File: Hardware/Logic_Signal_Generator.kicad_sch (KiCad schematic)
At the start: 10 parts, among them J1 JTAG, J3 USB_B, U1 PIC18F25K50-xSO

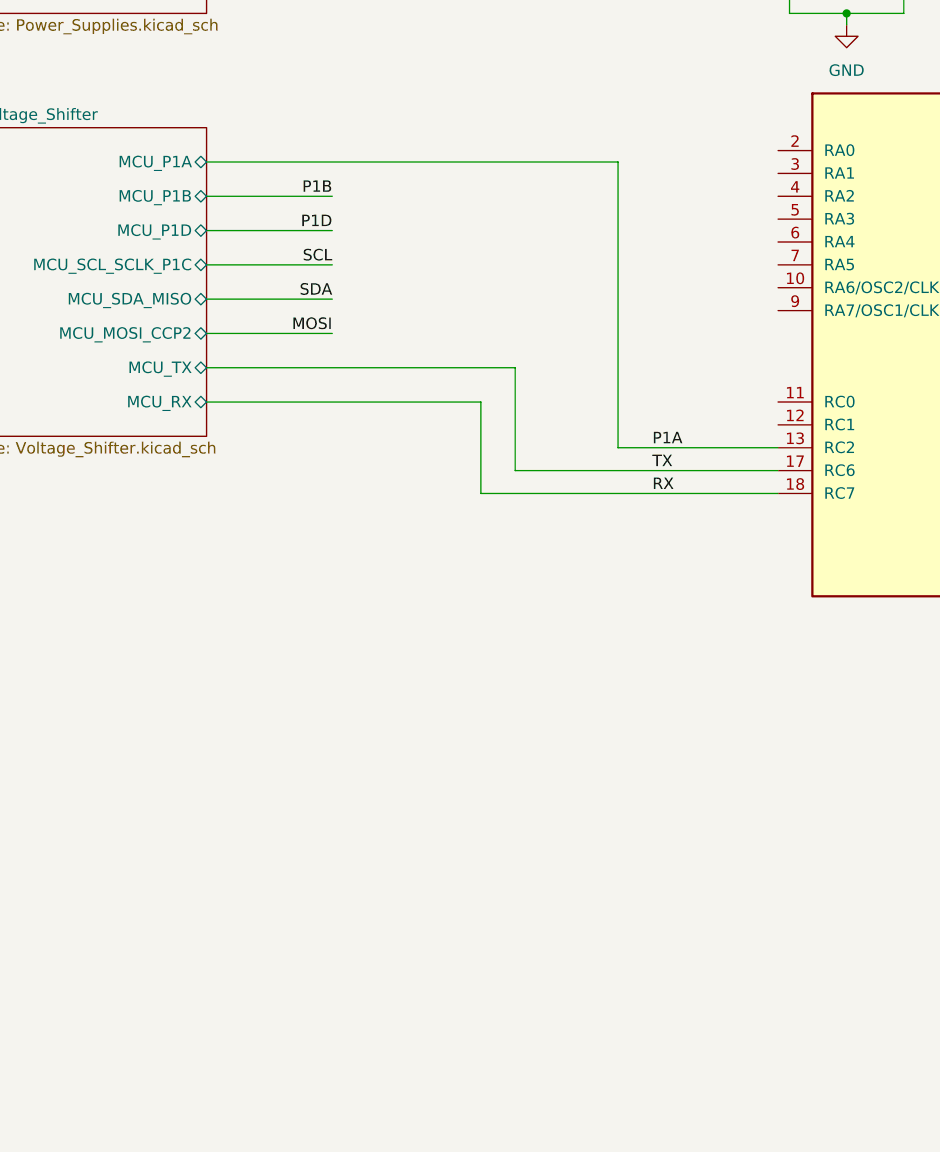
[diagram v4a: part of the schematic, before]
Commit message: [Hardware] Added the power and USB activity LEDs to the schematic.
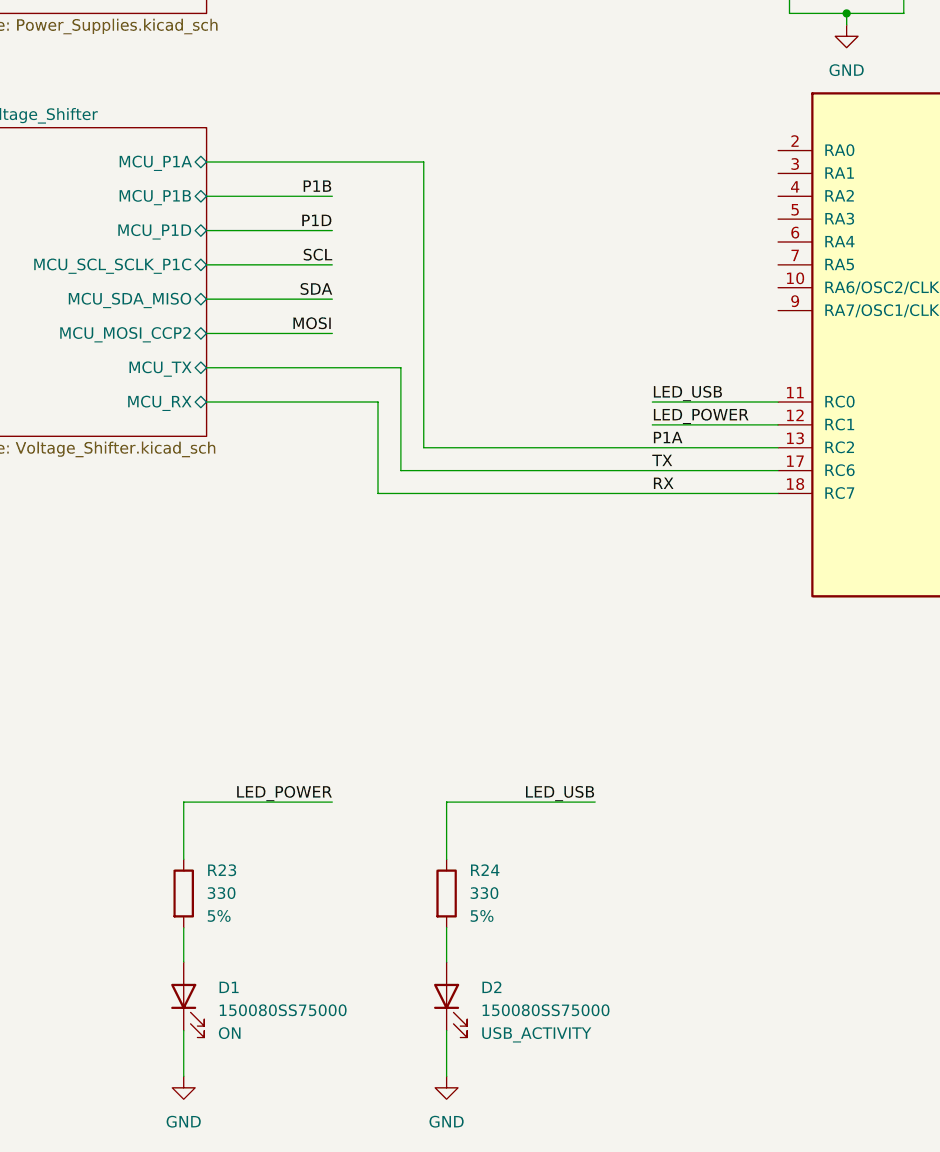
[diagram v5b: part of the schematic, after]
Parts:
- added D1, D2: 150080SS75000, LED_SMD:LED_0805_2012Metric_Pad1.15x1.40mm_HandSolder, symbol Device:LED
- added R23, R24: 330, Resistor_SMD:R_0603_1608Metric_Pad0.98x0.95mm_HandSolder, symbol Device:R
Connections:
- net GND: now also D1.1 (K), D2.1 (K)
- net LED_USB: now reaches U1.11 (RC0)
- net LED_USB: now also R24.1
- net LED_POWER: now reaches U1.12 (RC1)
- net LED_POWER: now also R23.1
- new net: D2.2 (A), R24.2
- new net: D1.2 (A), R23.2

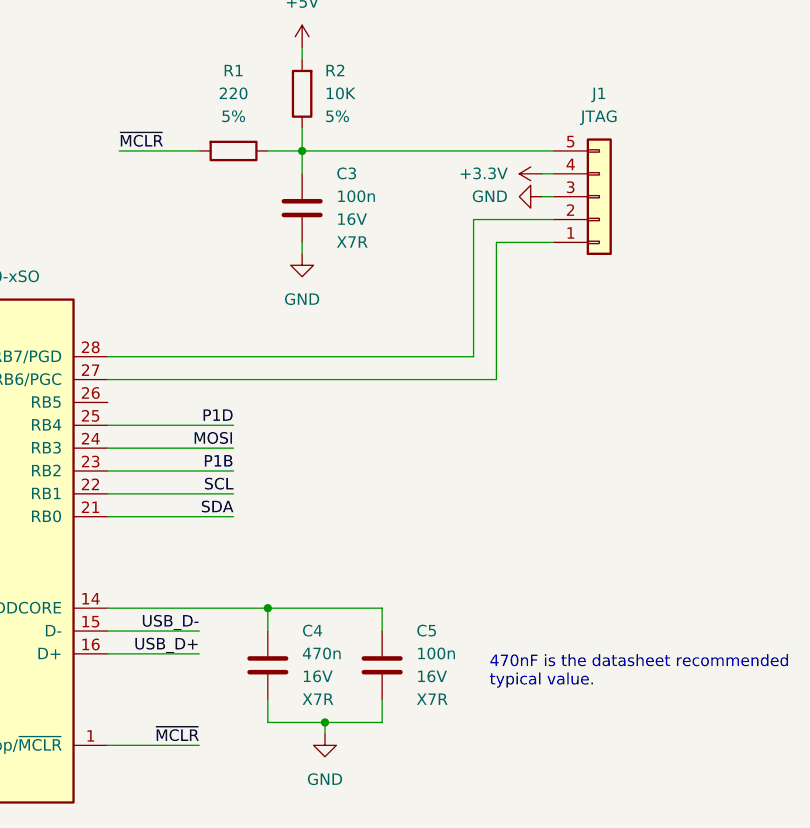
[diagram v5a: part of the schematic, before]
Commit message: [Hardware] Made an initial placement of the components on the PCB.
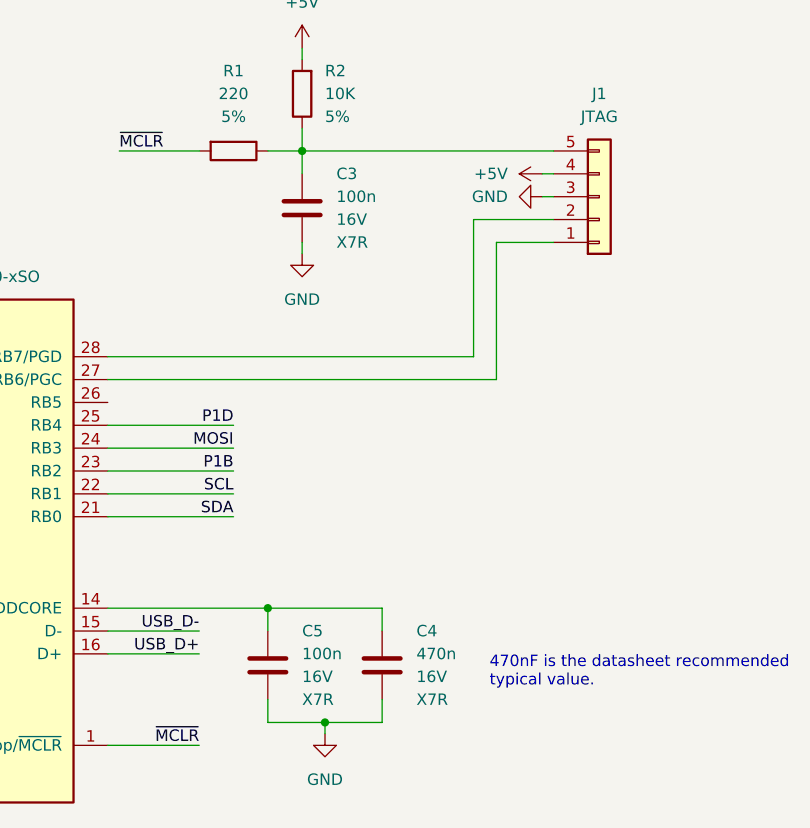
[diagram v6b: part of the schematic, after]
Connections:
- net +3.3V is gone; now on net +5V: J1.4 (Pin_4)
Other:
- moved on the sheet: C4, C5
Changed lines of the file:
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@@
+	)
+	(symbol
+		(lib_id "power:+5V")
+		(at 213.36 45.72 90)
+		(unit 1)
+		(exclude_from_sim no)
+		(in_bom yes)
+		(on_board yes)
+		(dnp no)
+		(fields_autoplaced yes)
+		(property "Reference" "#PWR039"
+			(at 217.17 45.72 0)
+			(effects
+				(font
+					(size 1.27 1.27)
+				)
+				(hide yes)
+			)
+		)
+		(property "Value" "+5V"
+			(at 209.55 45.7199 90)
+			(effects
+				(font
+					(size 1.27 1.27)
+				)
+				(justify left)
+			)
+		)
+		(property "Footprint" ""
+			(at 213.36 45.72 0)
+			(effects
+				(font
+					(size 1.27 1.27)
+				)
+				(hide yes)
+			)
+		)
+		(property "Datasheet" ""
+			(at 213.36 45.72 0)
+			(effects
+				(font
+					(size 1.27 1.27)
+				)
+				(hide yes)
+			)
+		)
+		(property "Description" "Power symbol creates a global label with name \"+5V\""
+			(at 213.36 45.72 0)
+			(effects
+				(font
+					(size 1.27 1.27)
+				)
+				(hide yes)
+			)
+		)
+		(pin "1"
+		)
+		(instances
+			(project "Logic_Signal_Generator"
+				(path "/24489a00-9deb-415a-805c-b5419253b078"
+					(reference "#PWR039")
+					(unit 1)
+				)
+			)
+		)
 	)
 	(symbol
@@
 	(symbol
 		(lib_id "Device:C")
-		(at 195.58 100.33 0)
+		(at 182.88 100.33 0)
 		(unit 1)
 		(exclude_from_sim no)
@@
 		(fields_autoplaced yes)
 		(property "Reference" "C5"
-			(at 199.39 96.5199 0)
+			(at 186.69 96.5199 0)
 			(effects
 				(font
@@
 		)
 		(property "Value" "100n"
-			(at 199.39 99.0599 0)
+			(at 186.69 99.0599 0)
 			(effects
 				(font
@@
 		)
 		(property "Footprint" "Capacitor_SMD:C_0603_1608Metric_Pad1.08x0.95mm_HandSolder"
-			(at 196.5452 104.14 0)
+			(at 183.8452 104.14 0)
 			(effects
 				(font
@@
 		)
 		(property "Datasheet" "~"
-			(at 195.58 100.33 0)
+			(at 182.88 100.33 0)
 			(effects
 				(font
@@
 		)
 		(property "Description" ""
-			(at 195.58 100.33 0)
+			(at 182.88 100.33 0)
 			(effects
 				(font
@@
 		)
 		(property "Value2" "16V"
-			(at 199.39 101.5999 0)
+			(at 186.69 101.5999 0)
 			(effects
 				(font
@@
 		)
 		(property "Value3" "X7R"
-			(at 199.39 104.1399 0)
+			(at 186.69 104.1399 0)
 			(effects
 				(font
@@
 	)
 	(symbol
-		(lib_id "power:+3.3V")
-		(at 213.36 45.72 90)
-		(unit 1)
-		(exclude_from_sim no)
-		(in_bom yes)
-		(on_board yes)
-		(dnp no)
-		(fields_autoplaced yes)
-		(property "Reference" "#PWR039"
-			(at 217.17 45.72 0)
-			(effects
-				(font
-					(size 1.27 1.27)
-				)
-				(hide yes)
-			)
-		)
-		(property "Value" "+3.3V"
-			(at 209.55 45.72 90)
-			(effects
-				(font
-					(size 1.27 1.27)
-				)
-				(justify left)
-			)
-		)
-		(property "Footprint" ""
-			(at 213.36 45.72 0)
-			(effects
-				(font
-					(size 1.27 1.27)
-				)
-				(hide yes)
-			)
-		)
-		(property "Datasheet" ""
-			(at 213.36 45.72 0)
-			(effects
-				(font
-					(size 1.27 1.27)
-				)
-				(hide yes)
-			)
-		)
-		(property "Description" "Power symbol creates a global label with name \"+3.3V\""
-			(at 213.36 45.72 0)
-			(effects
-				(font
-					(size 1.27 1.27)
-				)
-				(hide yes)
-			)
-		)
-		(pin "1"
-		)
-		(instances
-			(project "Logic_Signal_Generator"
-				(path "/24489a00-9deb-415a-805c-b5419253b078"
-					(reference "#PWR039")
-					(unit 1)
-				)
-			)
-		)
-	)
-	(symbol
 		(lib_id "Device:C")
 		(at 186.69 49.53 0)
@@
 	(symbol
 		(lib_id "Device:C")
-		(at 182.88 100.33 0)
+		(at 195.58 100.33 0)
 		(unit 1)
 		(exclude_from_sim no)
@@
 		(fields_autoplaced yes)
 		(property "Reference" "C4"
-			(at 186.69 96.5199 0)
+			(at 199.39 96.5199 0)
 			(effects
 				(font
@@
 		)
 		(property "Value" "470n"
-			(at 186.69 99.0599 0)
+			(at 199.39 99.0599 0)
 			(effects
 				(font
@@
 		)
 		(property "Footprint" "Capacitor_SMD:C_0603_1608Metric_Pad1.08x0.95mm_HandSolder"
-			(at 183.8452 104.14 0)
+			(at 196.5452 104.14 0)
 			(effects
 				(font
@@
 		)
 		(property "Datasheet" "~"
-			(at 182.88 100.33 0)
+			(at 195.58 100.33 0)
 			(effects
 				(font
@@
 		)
 		(property "Description" "Unpolarized capacitor"
-			(at 182.88 100.33 0)
+			(at 195.58 100.33 0)
 			(effects
 				(font
@@
 		)
 		(property "Value2" "16V"
-			(at 186.69 101.5999 0)
+			(at 199.39 101.5999 0)
 			(effects
 				(font
@@
 		)
 		(property "Value3" "X7R"
-			(at 186.69 104.1399 0)
-			(effects
-				(font
+			(at 199.39 104.1399 0)
+			(effects
+				(font

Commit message: [Hardware] Added the mounting holes and the PCB edges.
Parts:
- added H1, H2, H3, H4: Hole, MountingHole:MountingHole_4.5mm_Pad_Via, symbol Mechanical:MountingHole_Pad
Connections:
- net GND: now also H1.1, H2.1, H3.1, H4.1

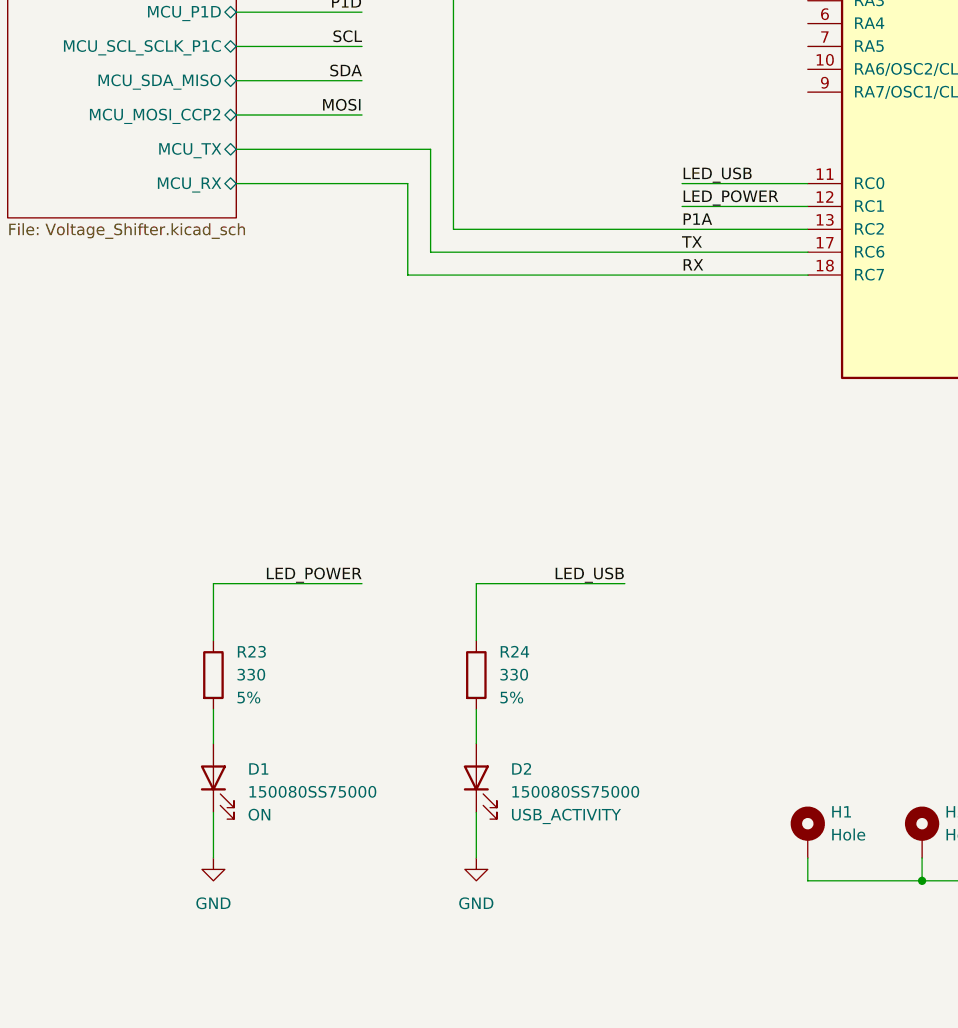
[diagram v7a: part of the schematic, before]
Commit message: [Hardware] Routed the LEDs and changed their current limiting resistors package.
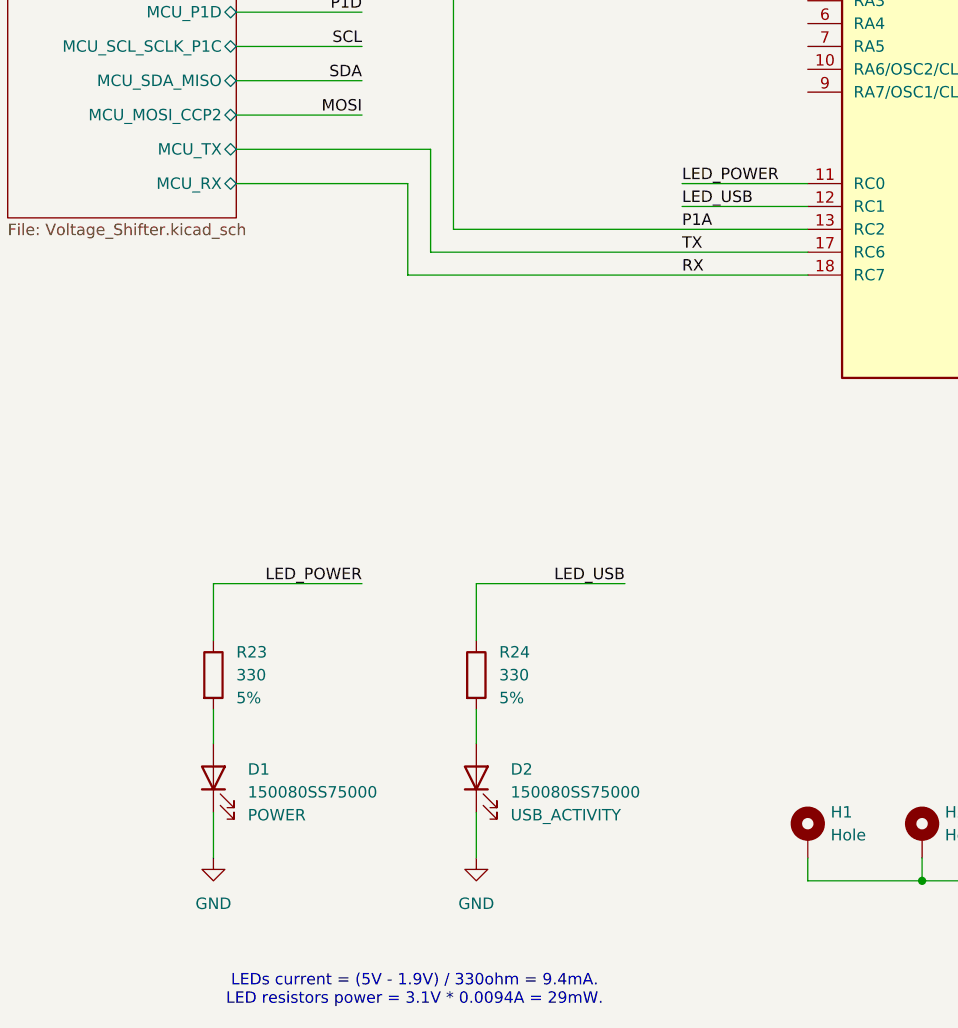
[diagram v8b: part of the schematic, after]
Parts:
- D1: Value2 ON -> POWER
- R23, R24: footprint Resistor_SMD:R_0603_1608Metric_Pad0.98x0.95mm_HandSolder -> Resistor_SMD:R_1206_3216Metric_Pad1.30x1.75mm_HandSolder
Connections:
- net LED_POWER: now also U1.11 (RC0); no longer U1.12 (RC1)
- net LED_USB: now also U1.12 (RC1); no longer U1.11 (RC0)
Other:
- note added: "LEDs current = (5V - 1.9V) / 330ohm = 9.4mA. LED resistors power = 3.1V * 0.0094A = 29mW."
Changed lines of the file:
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@@
 		(company "(C) Adrien RICCIARDI")
+	)
+	(text "LEDs current = (5V - 1.9V) / 330ohm = 9.4mA.\nLED resistors power = 3.1V * 0.0094A = 29mW."
+		(exclude_from_sim no)
+		(at 70.612 183.642 0)
+		(effects
+			(font
+				(size 1.27 1.27)
+			)
+		)
 	)
 	(text "470nF is the datasheet recommended\ntypical value."
@@
 	)
 	(label "LED_POWER"
+		(at 100.33 93.98 0)
+		(effects
+			(font
+				(size 1.27 1.27)
+			)
+			(justify left bottom)
+		)
+	)
+	(label "LED_USB"
 		(at 100.33 96.52 0)
-		(effects
-			(font
-				(size 1.27 1.27)
-			)
-			(justify left bottom)
-		)
-	)
-	(label "LED_USB"
-		(at 100.33 93.98 0)
 		(effects
 			(font
@@
 			)
 		)
-		(property "Footprint" "Resistor_SMD:R_0603_1608Metric_Pad0.98x0.95mm_HandSolder"
+		(property "Footprint" "Resistor_SMD:R_1206_3216Metric_Pad1.30x1.75mm_HandSolder"
 			(at 75.692 148.59 90)
 			(effects
@@
 			)
 		)
-		(property "Footprint" "Resistor_SMD:R_0603_1608Metric_Pad0.98x0.95mm_HandSolder"
+		(property "Footprint" "Resistor_SMD:R_1206_3216Metric_Pad1.30x1.75mm_HandSolder"
 			(at 46.482 148.59 90)
 			(effects
@@
 			)
 		)
-		(property "Value2" "ON"
+		(property "Value2" "POWER"
 			(at 52.07 164.1474 90)
 			(effects
